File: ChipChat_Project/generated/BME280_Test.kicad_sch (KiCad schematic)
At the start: 8 parts, among them U3 BME280

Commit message: 💾 snapshot 2026-02-19_17-31-37
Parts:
- removed R7, R8: 0R, symbol Device:R
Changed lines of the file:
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@@
 		(property "Datasheet" "" (at 152.39999999999998 88.9 0) (effects (font (size 1.27 1.27)) (hide yes)))
-	)
-	(symbol
-		(lib_id "Device:R")
-		(at 50.8 127.0 0)
-		(property "Reference" "R7" (at 50.8 129.54 0) (effects (font (size 1.27 1.27))))
-		(property "Value" "0R" (at 50.8 124.46 0) (effects (font (size 1.27 1.27))))
-		(property "Footprint" "" (at 50.8 127.0 0) (effects (font (size 1.27 1.27)) (hide yes)))
-		(property "Datasheet" "" (at 50.8 127.0 0) (effects (font (size 1.27 1.27)) (hide yes)))
-	)
-	(symbol
-		(lib_id "Device:R")
-		(at 101.6 127.0 0)
-		(property "Reference" "R8" (at 101.6 129.54 0) (effects (font (size 1.27 1.27))))
-		(property "Value" "0R" (at 101.6 124.46 0) (effects (font (size 1.27 1.27))))
-		(property "Footprint" "" (at 101.6 127.0 0) (effects (font (size 1.27 1.27)) (hide yes)))
-		(property "Datasheet" "" (at 101.6 127.0 0) (effects (font (size 1.27 1.27)) (hide yes)))
 	)
 	(hierarchical_label "I2C_SCL_BME"
@@
 	(wire
 		(pts
-			(xy 99.05999999999999 127.0) (xy 106.67999999999999 127.0)
-		)
-		(stroke
-			(width 0)
-			(type default)
-		)
-	)
-	(wire
-		(pts
-			(xy 106.67999999999999 127.0) (xy 162.56 127.0)
-		)
-		(stroke
-			(width 0)
-			(type default)
-		)
-	)
-	(wire
-		(pts
-			(xy 104.14 127.0) (xy 111.76 127.0)
-		)
-		(stroke
-			(width 0)
-			(type default)
-		)
-	)
-	(wire
-		(pts
-			(xy 111.76 127.0) (xy 162.56 127.0)
-		)
-		(stroke
-			(width 0)
-			(type default)
-		)
-	)
-	(wire
-		(pts
 			(xy 162.56 50.8) (xy 162.56 50.8)
-		)
-		(stroke
-			(width 0)
-			(type default)
-		)
-	)
-	(wire
-		(pts
-			(xy 162.56 50.8) (xy 162.56 127.0)
-		)
-		(stroke
-			(width 0)
-			(type default)
-		)
-	)
-	(wire
-		(pts
-			(xy 162.56 127.0) (xy 162.56 127.0)
 		)
 		(stroke
@@
 	(wire
 		(pts
-			(xy 48.26 127.0) (xy 55.879999999999995 127.0)
-		)
-		(stroke
-			(width 0)
-			(type default)
-		)
-	)
-	(wire
-		(pts
-			(xy 55.879999999999995 127.0) (xy 111.75999999999999 127.0)
-		)
-		(stroke
-			(width 0)
-			(type default)
-		)
-	)
-	(wire
-		(pts
-			(xy 53.339999999999996 127.0) (xy 60.959999999999994 127.0)
-		)
-		(stroke
-			(width 0)
-			(type default)
-		)
-	)
-	(wire
-		(pts
-			(xy 60.959999999999994 127.0) (xy 111.75999999999999 127.0)
-		)
-		(stroke
-			(width 0)
-			(type default)
-		)
-	)
-	(wire
-		(pts
 			(xy 111.75999999999999 48.26) (xy 111.75999999999999 50.8)
 		)
 		(stroke
-			(width 0)
-			(type default)
-		)
-	)
-	(wire
-		(pts
-			(xy 111.75999999999999 50.8) (xy 111.75999999999999 127.0)
-		)
-		(stroke
-			(width 0)
-			(type default)
-		)
-	)
-	(wire
-		(pts
-			(xy 111.75999999999999 127.0) (xy 111.75999999999999 127.0)
-		)
-		(stroke

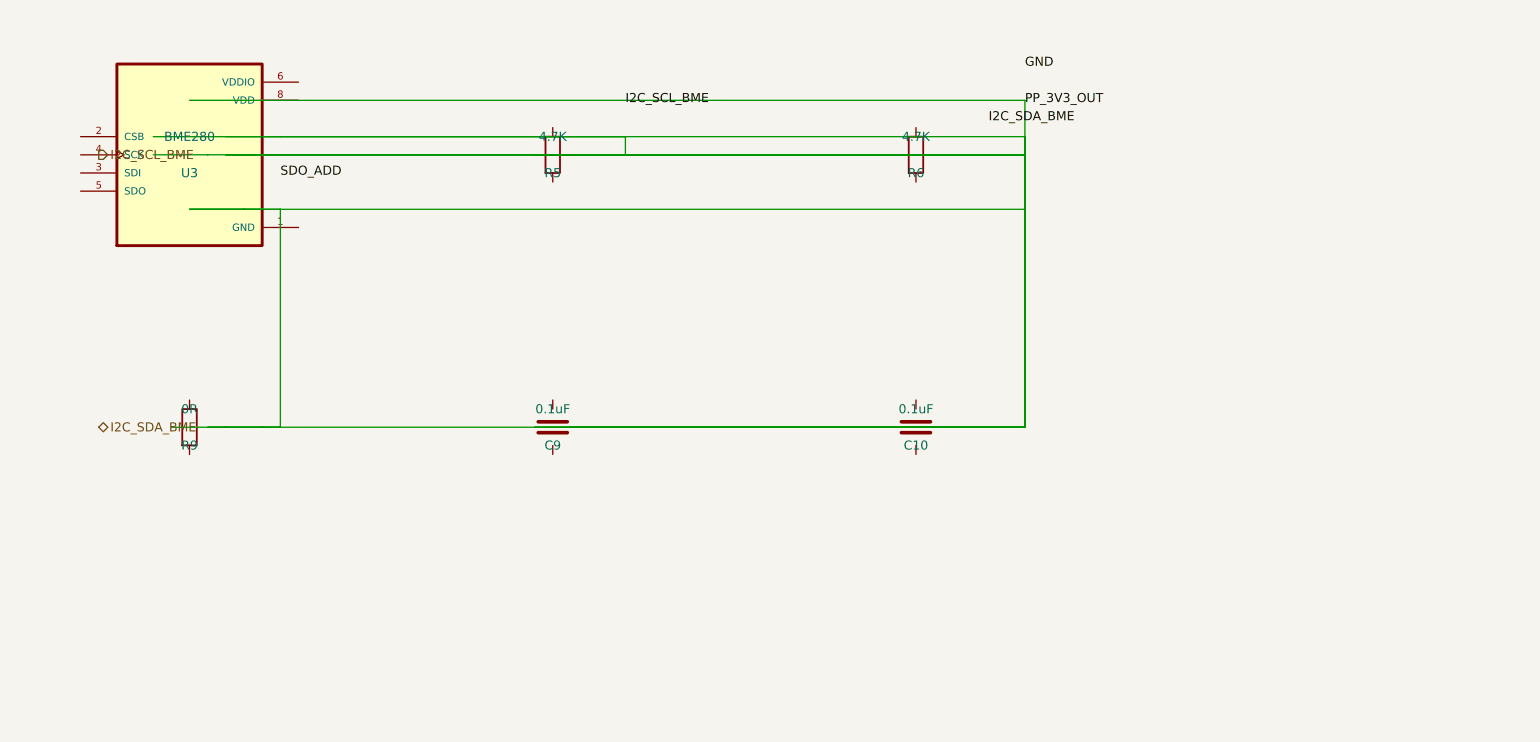
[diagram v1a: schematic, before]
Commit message: bme280test.py resistor in top left in correct config hopefully nothing breaks in the next one
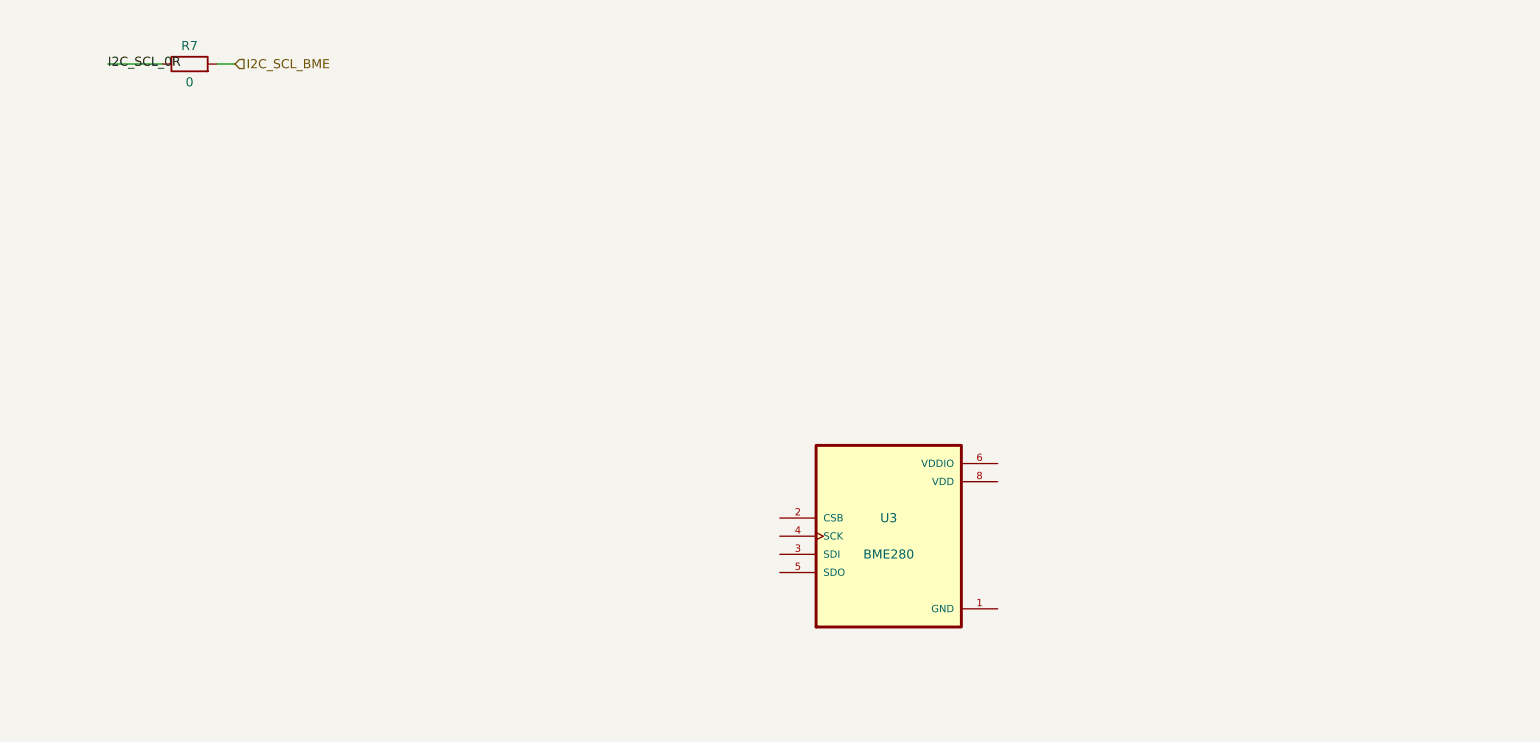
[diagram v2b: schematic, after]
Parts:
- removed C10, C9: 0.1uF, symbol Device:C
- removed R5, R6: 4.7K, symbol Device:R
- removed R9: 0R, symbol Device:R
- added R7: 0, symbol Resistor
- U3: footprint BME280 -> Package_LGA:Bosch_LGA-8_2.5x2.5mm_P0.65mm_ClockwisePinNumbering
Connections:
- net I2C_SCL_BME: now also R7.2
- new net I2C_SCL_0R: R7.1

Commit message: 💾 snapshot 2026-02-19_18-11-44
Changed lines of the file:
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@@
 	(wire
 		(pts
-			(xy 54.61 38.1) (xy 57.15 38.1)
+			(xy 54.61 38.1) (xy 62.23 38.1)
 		)
 		(stroke
@@
 	(hierarchical_label "I2C_SCL_BME"
 		(shape input)
-		(at 57.15 38.1 0)
+		(at 62.23 38.1 0)
 		(effects
 			(font
 				(size 1.27 1.27)
 			)
+			(justify left)
 		)
 	)
@@
 				(size 1.27 1.27)
 			)
+			(justify right bottom)
 		)
 	)

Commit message: 💾 snapshot 2026-02-19_18-48-47
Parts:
- added C10, C9: 0.1uF, symbol Capacitor
- added R5, R6: 4.7K, symbol Resistor
- added R8, R9: 0R, symbol Resistor
- R7: value 0 -> 0R
- U3: footprint Package_LGA:Bosch_LGA-8_2.5x2.5mm_P0.65mm_ClockwisePinNumbering -> (none)
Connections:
- net GND: now also C10.1, C9.1, R9.1
- net I2C_SCL_BME: now also R5.2
- new net I2C_SDA_0R: R8.1
- new net I2C_SDA_BME: R6.2, R8.2
- new net PP_3V3_OUT: C10.2, C9.2, R5.1, R6.1
- new net SDO_ADD: R9.2

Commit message: 💾 snapshot 2026-02-19_19-10-38
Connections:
- net PP_3V3_OUT is gone; now on net GND: C10.2, C9.2, R5.1, R6.1
- net GND: now also U3.6 (VDDIO)
- net I2C_SCL_0R: now also U3.4 (SCK)
- net I2C_SDA_0R: now also U3.2 (CSB)
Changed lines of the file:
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@@
+		)
+	)
+	(wire
+		(pts
+			(xy 215.24 89.84) (xy 222.86 89.84)
+		)
+		(stroke
+			(width 0)
+			(type default)
+		)
+	)
+	(label "GND"
+		(at 222.86 89.84 0)
+		(effects
+			(font
+				(size 1.27 1.27)
+			)
+			(justify left bottom)
+		)
+	)
+	(wire
+		(pts
+			(xy 184.76 97.46) (xy 177.14 97.46)
+		)
+		(stroke
+			(width 0)
+			(type default)
+		)
+	)
+	(label "I2C_SDA_0R"
+		(at 177.14 97.46 0)
+		(effects
+			(font
+				(size 1.27 1.27)
+			)
+			(justify right bottom)
+		)
+	)
+	(wire
+		(pts
+			(xy 184.76 100.0) (xy 177.14 100.0)
+		)
+		(stroke
+			(width 0)
+			(type default)
+		)
+	)
+	(label "I2C_SCL_0R"
+		(at 177.14 100.0 0)
+		(effects
+			(font
+				(size 1.27 1.27)
+			)
+			(justify right bottom)
+		)
+	)
+	(wire
+		(pts
+			(xy 184.76 94.92) (xy 177.14 94.92)
+		)
+		(stroke
+			(width 0)
+			(type default)
+		)
+	)
+	(label "SDO_ADD"
+		(at 177.14 94.92 0)
+		(effects
+			(font
+				(size 1.27 1.27)
+			)
+			(justify right bottom)
+		)
+	)
+	(wire
+		(pts
+			(xy 215.24 110.16) (xy 222.86 110.16)
+		)
+		(stroke
+			(width 0)
+			(type default)
+		)
+	)
+	(hierarchical_label "PP_3V3_OUT"
+		(shape bidirectional)
+		(at 222.86 110.16 0)
+		(effects
+			(font
+				(size 1.27 1.27)
+			)
+			(justify left)
+		)
+	)
+	(wire
+		(pts
+			(xy 215.24 107.62) (xy 222.86 107.62)
+		)
+		(stroke
+			(width 0)
+			(type default)
+		)
+	)
+	(hierarchical_label "PP_3V3_OUT"
+		(shape bidirectional)
+		(at 222.86 107.62 0)
+		(effects
+			(font
+				(size 1.27 1.27)
+			)
+			(justify left)
 		)
 	)

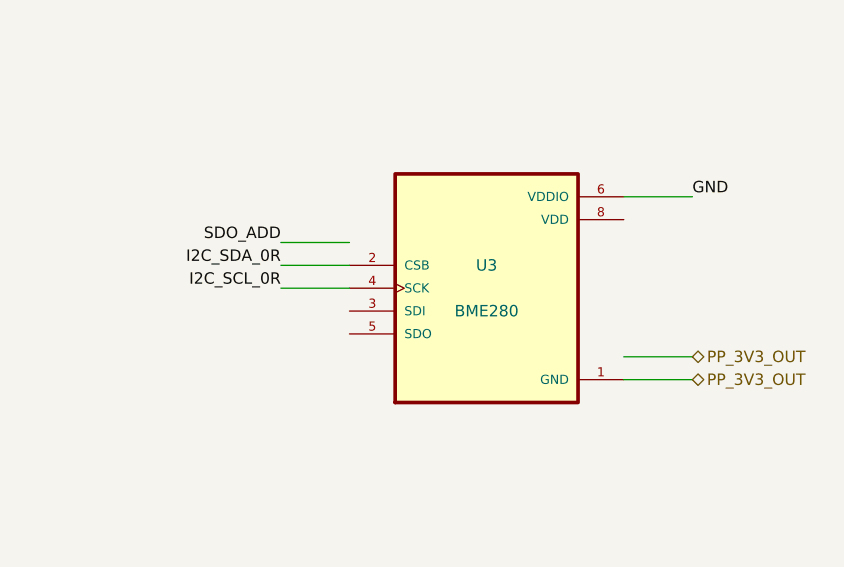
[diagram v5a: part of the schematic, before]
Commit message: mcp2210-a algorithmically gets placed from dummy.json toogit add .
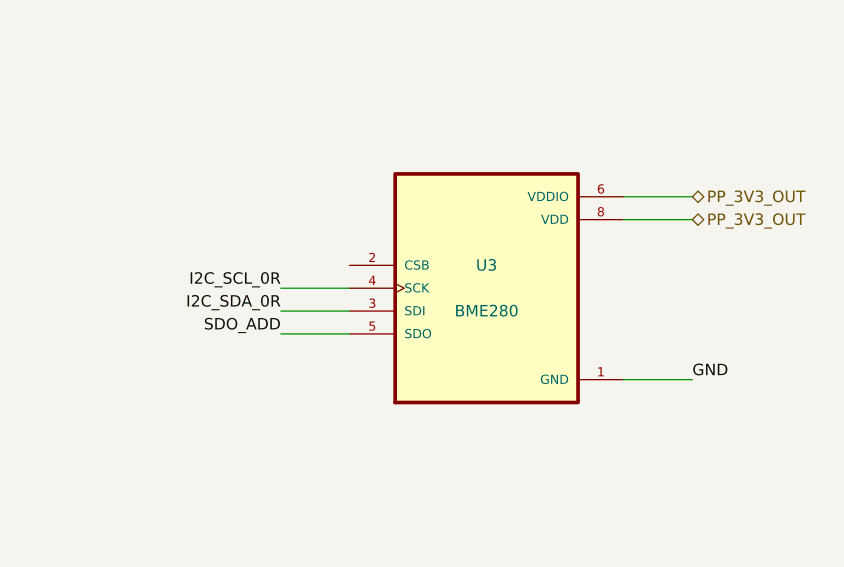
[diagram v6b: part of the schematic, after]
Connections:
- net GND: no longer C10.2, C9.2, R5.1, R6.1, U3.6 (VDDIO)
- net I2C_SDA_0R: now also U3.3 (SDI); no longer U3.2 (CSB)
- net SDO_ADD: now also U3.5 (SDO)
- net PP_3V3_OUT: now reaches U3.8 (VDD)
- net PP_3V3_OUT: now also C10.2, C9.2, R5.1, R6.1, U3.6 (VDDIO)
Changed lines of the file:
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@@
 	(wire
 		(pts
-			(xy 215.24 89.84) (xy 222.86 89.84)
+			(xy 215.24 110.16) (xy 222.86 110.16)
 		)
 		(stroke
@@
 	)
 	(label "GND"
-		(at 222.86 89.84 0)
+		(at 222.86 110.16 0)
 		(effects
 			(font
@@
 	(wire
 		(pts
-			(xy 184.76 97.46) (xy 177.14 97.46)
+			(xy 184.76 102.54) (xy 177.14 102.54)
 		)
 		(stroke
@@
 	)
 	(label "I2C_SDA_0R"
-		(at 177.14 97.46 0)
+		(at 177.14 102.54 0)
 		(effects
 			(font
@@
 	(wire
 		(pts
-			(xy 184.76 94.92) (xy 177.14 94.92)
+			(xy 184.76 105.08) (xy 177.14 105.08)
 		)
 		(stroke
@@
 	)
 	(label "SDO_ADD"
-		(at 177.14 94.92 0)
+		(at 177.14 105.08 0)
 		(effects
 			(font
@@
 	(wire
 		(pts
-			(xy 215.24 110.16) (xy 222.86 110.16)
+			(xy 215.24 89.84) (xy 222.86 89.84)
 		)
 		(stroke
@@
 	(hierarchical_label "PP_3V3_OUT"
 		(shape bidirectional)
-		(at 222.86 110.16 0)
+		(at 222.86 89.84 0)
 		(effects
 			(font
@@
 	(wire
 		(pts
-			(xy 215.24 107.62) (xy 222.86 107.62)
+			(xy 215.24 92.38) (xy 222.86 92.38)
 		)
 		(stroke
@@
 	(hierarchical_label "PP_3V3_OUT"
 		(shape bidirectional)
-		(at 222.86 107.62 0)
+		(at 222.86 92.38 0)
 		(effects
 			(font
